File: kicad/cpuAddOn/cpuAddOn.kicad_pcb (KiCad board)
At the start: 6 copper layers, 60.6 x 100 mm, 138 parts, among them J1 QTE-020-01-X-D-A, J2 105450-0101, J3 Conn_01x05_Pin, J4 SJ-3551B-MSMT-TR-67, J5 TE_2311765-1, J7 Conn_02x13_Odd_Even, SW1 B3U-1000P[], SW2 B3U-1000P[], SW3 B3U-1000P[], SW4 B3U-1000P[]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

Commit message: Small revision on PCB
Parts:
- moved C23 1.45 mm to (101.7, 119.1)
- moved C24 1.45 mm to (102.4, 111.3)
- moved C26 1.45 mm to (94.2, 116.3)
- moved C27 1.45 mm to (98.0, 116.3)
- moved C28 1.45 mm to (99.9, 116.3)
- moved C29 1.45 mm to (93.2, 115.3)
- moved C30 1.45 mm to (93.2, 114.3)
- moved C31 1.45 mm to (93.2, 113.3)
- moved C32 1.45 mm to (93.2, 112.3)
- moved C34 1.45 mm to (104.0, 112.7)
- moved C38 1.45 mm to (91.0, 113.0)
- moved R28 1.45 mm to (104.6, 130.5)
- moved R29 1.45 mm to (96.1, 116.3)
- moved R30 1.45 mm to (102.7, 119.1)
- moved U9 1.45 mm to (98.4, 119.4)
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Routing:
- net CodecSDin: track 31.4 -> 64.6 mm
- net GND: track 222.6 -> 219.6 mm, vias 112 -> 111
- net Net-(U9-SLEEVE): track 22.2 -> 23.8 mm
- net SCL: track 90.6 -> 89.0 mm
- net SDA: track 103.5 -> 101.9 mm
- net Net-(U10-ROUTP): track 26.7 -> 28.2 mm
- net Net-(U10-LOUTP): track 22.8 -> 24.2 mm
- net Net-(U9-RING2): track 26.2 -> 27.7 mm
- net Net-(U3-PB2/BOOT1): track 4.21 -> 5.61 mm
- net Clock24MHz: track 111.4 -> 110.1 mm
- net Net-(U3-PB11): track 21.2 -> 22.2 mm
- net Presure_Irq: track 84.1 -> 84.7 mm
- net Net-(U10-JACKSNS/AUX): track 22.6 -> 23.1 mm
- net CodecSDout: track 30.4 -> 29.9 mm
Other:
- outline, holes or cut-outs redrawn

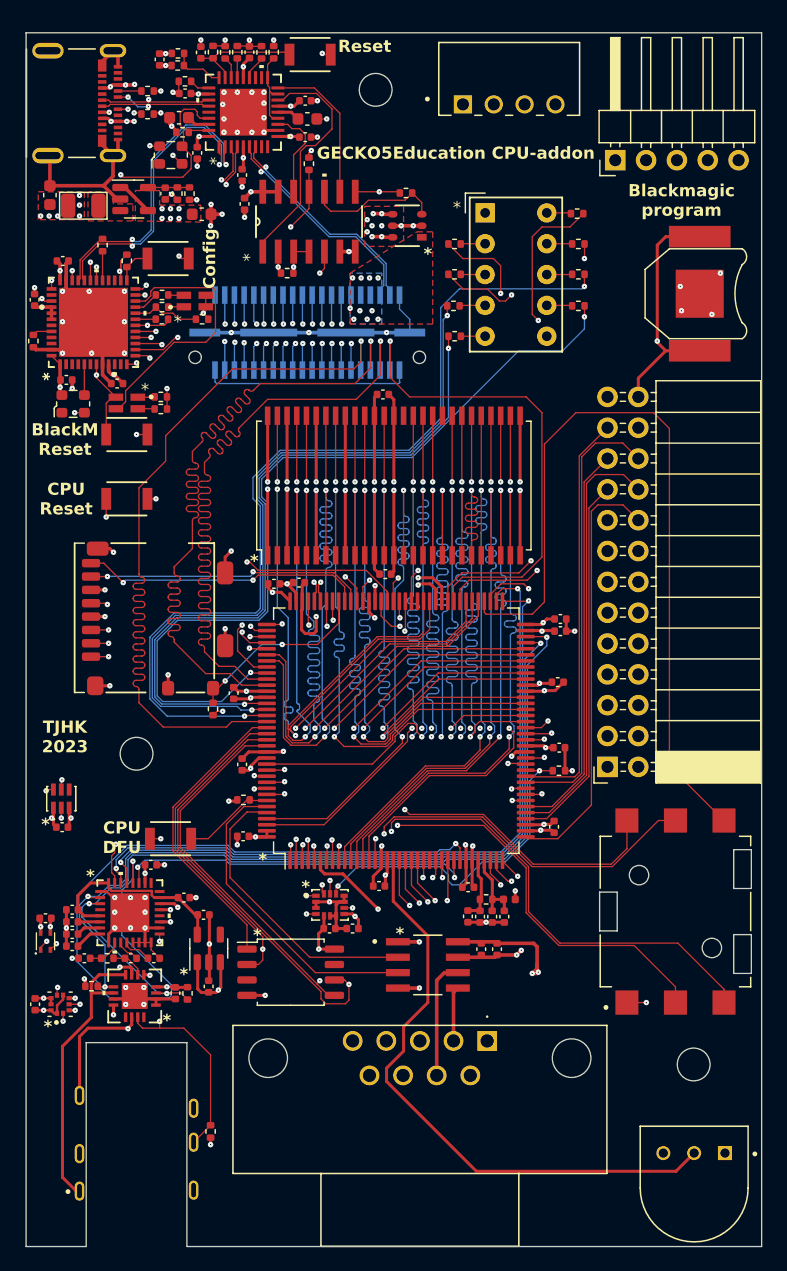
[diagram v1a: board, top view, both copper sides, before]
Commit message: fixed bug with RS232 Added support for bigger SDRAMs Changed 7-segment display to SMD and active low
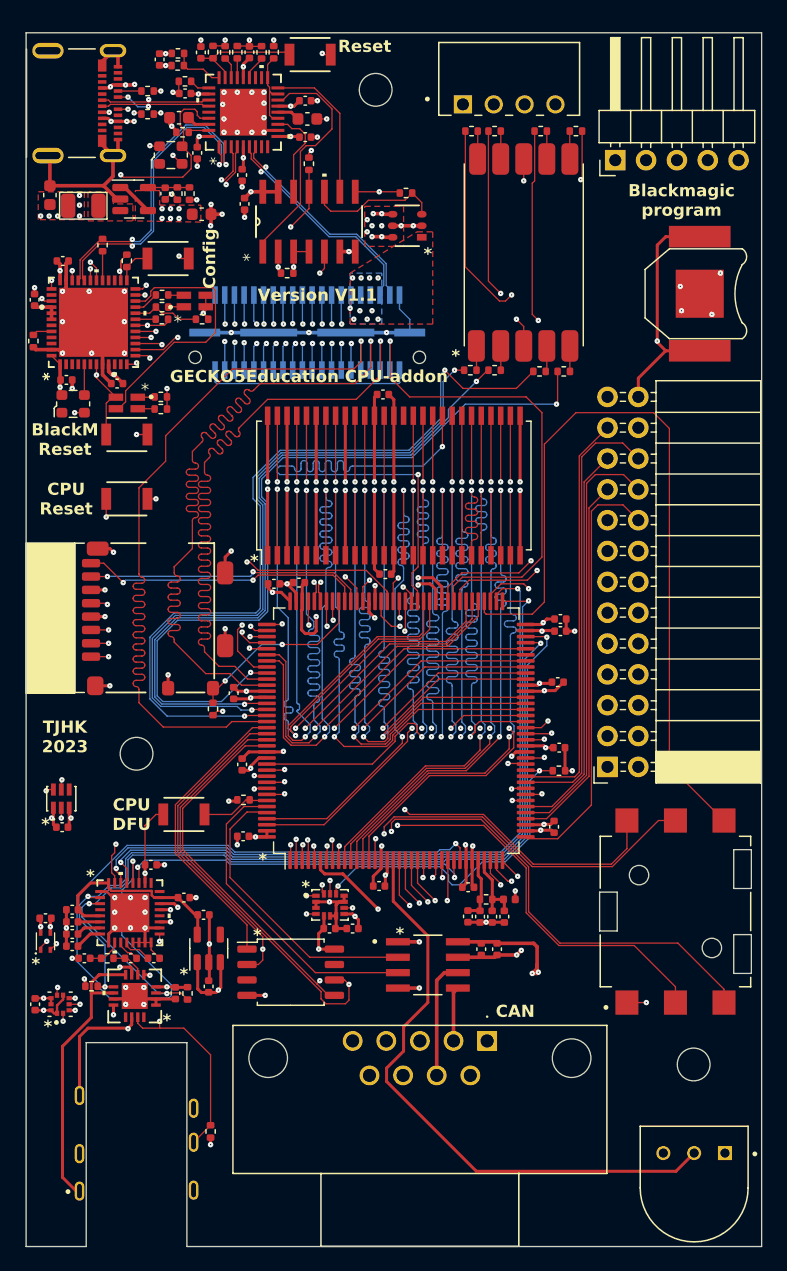
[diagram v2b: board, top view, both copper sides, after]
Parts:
- R35, R36, R37, R38, R39, R40, R41, R42: value 75R -> 62R
- U16: value HDSP-7403 -> HDSM-431W; footprint Display_7Segment:HDSP-7401 -> cpuAddOn:HDSM-431W
- U7: value AS4C4M16SA-6TAN -> AS4C16M16SA-6TAN
- moved R41 11.9 mm to (126.1, 48.1)
- moved U16 11.0 mm to (126.6, 65.8)
- moved R40 9.87 mm to (128.0, 48.1)
- moved R36 9.30 mm to (134.7, 48.1)
- moved R37 8.62 mm to (131.7, 67.9), turned to 0 degrees
- moved R35 7.43 mm to (131.8, 48.1), turned to 0 degrees
- moved R42 5.53 mm to (133.7, 67.9), turned to 0 degrees
- moved R39 5.48 mm to (126.0, 67.8)
- moved R38 4.32 mm to (128.0, 67.8)
- moved SW5 2.28 mm to (102.4, 104.4), turned to 180 degrees
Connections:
- SW5 pad 1: +3.3V -> Net-(U6-BOOT0)
- SW5 pad 2: Net-(U6-BOOT0) -> +3.3V
- U16 pad 1: GND -> Net-(U16-E)
- U16 pad 10: Net-(U16-A) -> Net-(U16-G)
- U16 pad 2: Net-(U16-F) -> Net-(U16-D)
- U16 pad 3: Net-(U16-G) -> +3.3V
- U16 pad 4: Net-(U16-E) -> Net-(U16-C)
- U16 pad 5: Net-(U16-D) -> Net-(U16-DP)
- U16 pad 6: GND -> Net-(U16-B)
- U16 pad 7: Net-(U16-DP) -> Net-(U16-A)
- U16 pad 8: Net-(U16-C) -> +3.3V
- U16 pad 9: Net-(U16-B) -> Net-(U16-F)
- U6 pad 101: BlackRxd -> BlackTxd
- U6 pad 102: BlackTxd -> BlackRxd
- U7 pad 36: unconnected-(U7-NC-Pad36) -> FMC_A12
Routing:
- net FMC_A12: track 0.00 -> 45.7 mm, vias 0 -> 2
- net Seg_C: track 76.6 -> 66.5 mm
- net Seg_G: track 42.4 -> 52.5 mm
- net +3.3V: track 144.6 -> 153.1 mm, vias 62 -> 63
- net Seg_B: track 39.0 -> 46.1 mm
- net Seg_F: track 45.1 -> 51.6 mm
- net Seg_E: track 62.8 -> 58.5 mm
- net Seg_DP: track 69.6 -> 65.7 mm
- net Seg_A: track 41.0 -> 44.8 mm
- net Net-(U6-BOOT0): track 7.51 -> 5.58 mm
- net Seg_D: track 59.8 -> 58.4 mm
- net Motion_Int1: track 55.8 -> 55.2 mm
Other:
- board text added: "CAN"
- board text added: "Version V1.1"

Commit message: Made V1.1 of the cpu-addon
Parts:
- added C56: 9pF, Capacitor_SMD:C_0402_1005Metric, F.Cu at (114.2, 112.3)
- added C57: 9pF, Capacitor_SMD:C_0402_1005Metric, F.Cu at (115.6, 112.3)
- added Y1: RT2012-32.768-9-20-EXT-TR, Crystal:Crystal_SMD_2012-2Pin_2.0x1.2mm, F.Cu at (114.9, 110.4)
- BT1: footprint Battery:BatteryHolder_Keystone_2998_1x6.8mm -> Battery:BatteryHolder_Keystone_1060_1x2032; moved to B.Cu
- J7: value Conn_02x13_Odd_Even -> Conn_02x16_Odd_Even; footprint Connector_PinSocket_2.54mm:PinSocket_2x13_P2.54mm_Horizontal -> Connector_PinSocket_2.54mm:PinSocket_2x16_P2.54mm_Horizontal
- U16: value HDSM-431W -> HDSM-433C
- moved BT1 55.3 mm to (119.0, 110.3), turned to 0 degrees
- moved C35 6.26 mm to (108.3, 112.5)
- moved C36 6.26 mm to (110.2, 112.5)
- moved U13 6.26 mm to (108.3, 110.5)
- moved C51 0.58 mm to (118.9, 110.7), turned to -90 degrees
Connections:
- J7 pad 1: GPIO1 -> +3.3V
- J7 pad 10: GPIO10 -> PMOD1_8
- J7 pad 11: GPIO11 -> PMOD1_1
- J7 pad 12: GPIO12 -> PMOD1_7
- J7 pad 13: GPIO13 -> ADC_PWM1
- J7 pad 14: GPIO14 -> ADC_PWM0
- J7 pad 15: GPIO15 -> ADC_PWM3
- J7 pad 16: GPIO16 -> ADC_PWM2
- J7 pad 17: GPIO17 -> ADC4
- J7 pad 18: GPIO18 -> GND
- J7 pad 19: GPIO19 -> +3.3V
- J7 pad 2: GPIO2 -> +3.3V
- J7 pad 20: GPIO20 -> +3.3V
- J7 pad 21: GPIO21 -> GND
- J7 pad 22: GPIO22 -> GND
- J7 pad 23: GPIO23 -> PMOD2_4
- J7 pad 24: +3.3V -> PMOD2_10
- J7 pad 25: GND -> PMOD2_3
- J7 pad 26: Net-(BT1-+) -> PMOD2_9
- J7 pad 3: GPIO3 -> GND
- J7 pad 4: GPIO4 -> GND
- J7 pad 5: GPIO5 -> PMOD1_4
- J7 pad 6: GPIO6 -> PMOD1_10
- J7 pad 7: GPIO7 -> PMOD1_3
- J7 pad 8: GPIO8 -> PMOD1_9
- J7 pad 9: GPIO9 -> PMOD1_2
- U16 pad 3: +3.3V -> GND
- U16 pad 8: +3.3V -> GND
- U6 pad 1: GPIO1 -> Joy3
- U6 pad 135: Joy3 -> PMOD1_2
- U6 pad 136: Joy4 -> PMOD1_9
- U6 pad 137: Joy5 -> PMOD1_10
- U6 pad 19: GPIO14 -> ADC4
- U6 pad 2: GPIO2 -> Joy4
- U6 pad 20: GPIO13 -> ADC_PWM2
- U6 pad 21: GPIO12 -> ADC_PWM3
- U6 pad 22: GPIO11 -> PMOD2_10
- U6 pad 26: GPIO10 -> PMOD2_9
- U6 pad 27: GPIO9 -> PMOD2_8
- U6 pad 3: GPIO3 -> Joy5
- U6 pad 34: GPIO15 -> PMOD2_1
- U6 pad 35: GPIO16 -> PMOD2_4
- U6 pad 36: GPIO17 -> PMOD2_2
- U6 pad 37: GPIO18 -> PMOD2_3
- U6 pad 4: GPIO4 -> PMOD1_7
- U6 pad 40: GPIO19 -> PMOD1_1
- U6 pad 41: GPIO20 -> PMOD1_4
- U6 pad 42: GPIO21 -> PMOD1_3
- U6 pad 46: GPIO22 -> ADC_PWM0
- U6 pad 47: GPIO23 -> ADC_PWM1
- U6 pad 5: GPIO5 -> PMOD1_8
- U6 pad 7: GPIO6 -> PMOD2_7
- U6 pad 8: GPIO7 -> Net-(U6-PC14)
- U6 pad 9: GPIO8 -> Net-(U6-PC15)
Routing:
- net PMOD2_7: track 0.00 -> 82.5 mm, vias 0 -> 1
- net PMOD2_8: track 0.00 -> 61.6 mm, vias 0 -> 1
- net PMOD2_9: track 0.00 -> 60.1 mm, vias 0 -> 1
- net PMOD2_10: track 0.00 -> 57.0 mm, vias 0 -> 1
- net ADC4: track 0.00 -> 54.8 mm, vias 0 -> 1
- net PMOD2_1: track 0.00 -> 52.4 mm, vias 0 -> 1
- net PMOD1_7: track 0.00 -> 52.2 mm, vias 0 -> 1
- net GPIO13: track 48.9 -> 0.00 mm, vias 1 -> 0
- net PMOD2_2: track 0.00 -> 48.5 mm, vias 0 -> 1
- net GPIO14: track 48.5 -> 0.00 mm, vias 1 -> 0
- net ADC_PWM3: track 0.00 -> 47.9 mm, vias 0 -> 1
- net ADC_PWM2: track 0.00 -> 47.7 mm, vias 0 -> 1
- net PMOD2_3: track 0.00 -> 47.2 mm
- net PMOD1_8: track 0.00 -> 46.7 mm, vias 0 -> 1
- net PMOD1_2: track 0.00 -> 45.1 mm, vias 0 -> 1
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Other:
- board text added: "+3V3"
- board text added: "GND"
- board text added: "PMOD1"
- board text added: "PMOD2"
- board text added: "SWCLK"
- board text added: "SWDIO"
- board text added: "SWO"

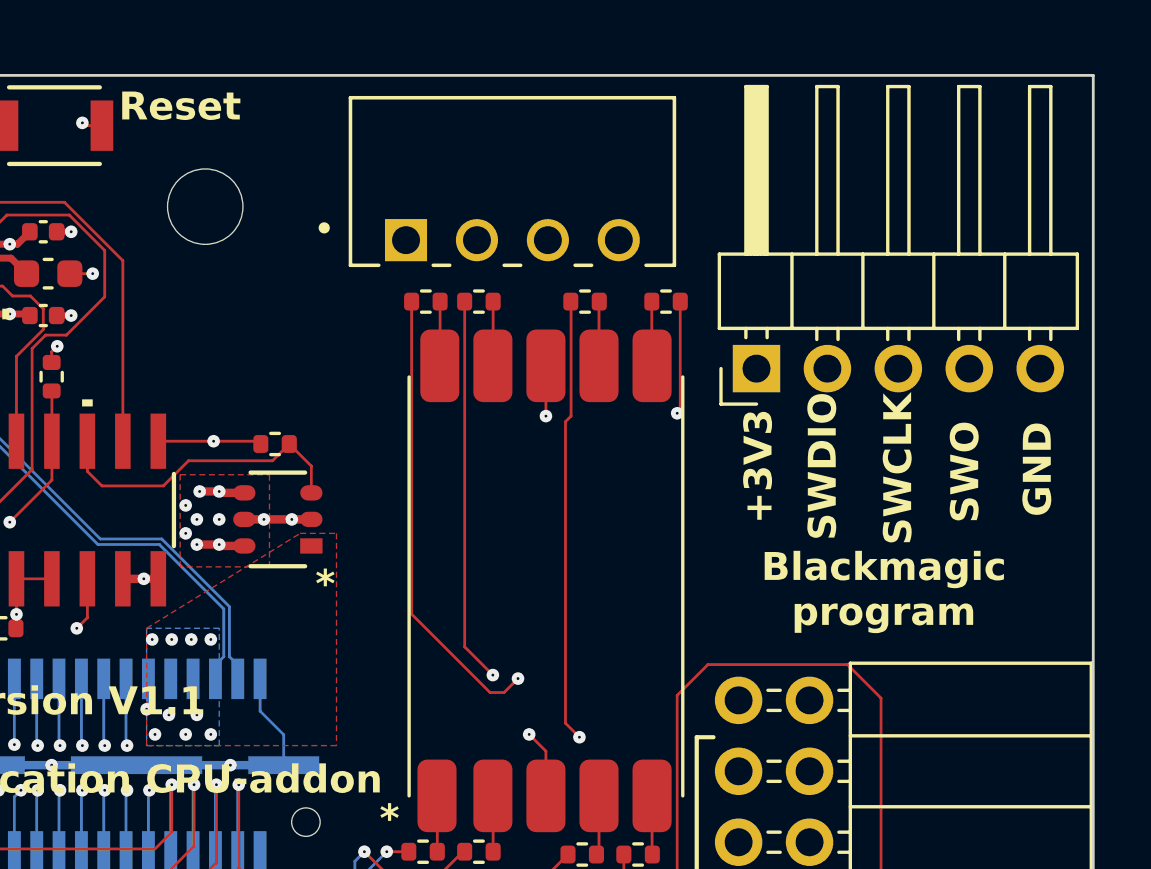
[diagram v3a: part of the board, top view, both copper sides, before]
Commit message: Added 2 add-on boards and updated GECKO5 to support olimex camera-OV7670 and an RTC.
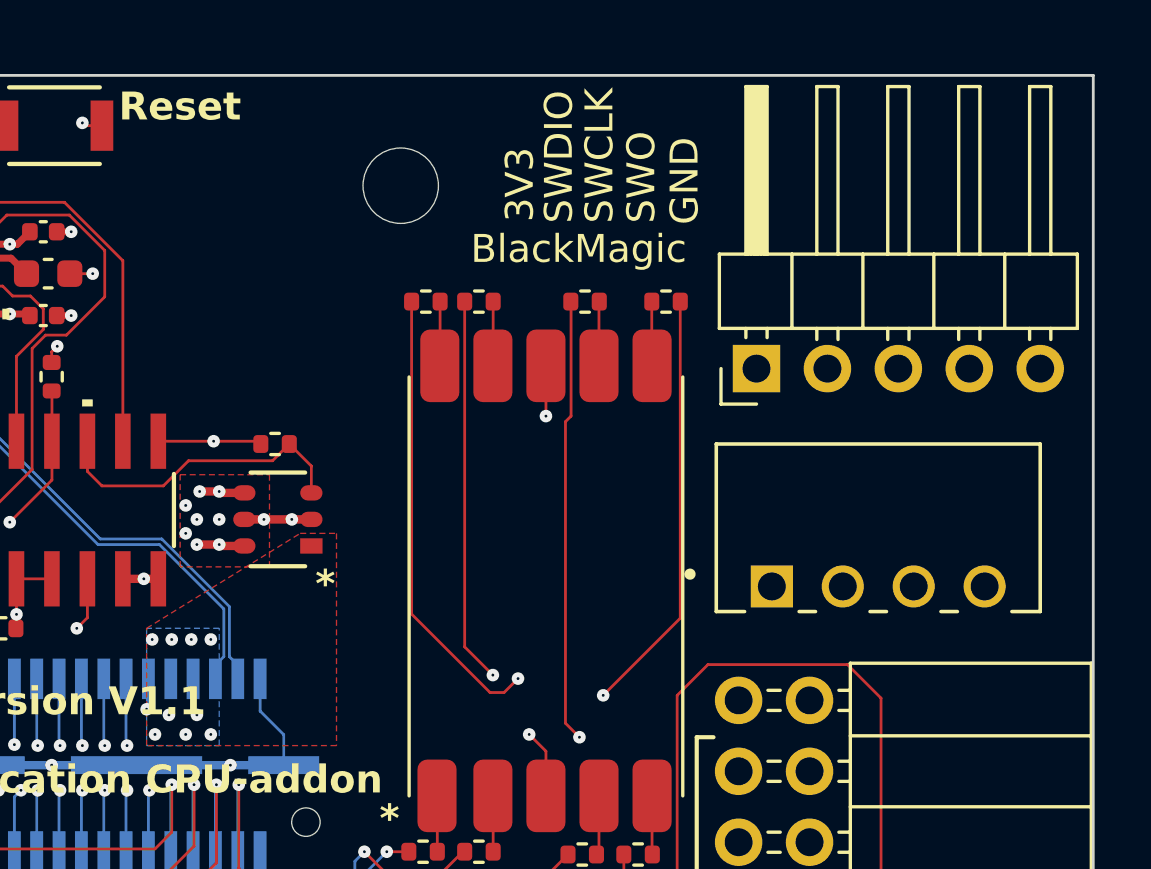
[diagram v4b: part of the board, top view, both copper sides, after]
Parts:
- moved PS1 18.0 mm to (142.3, 56.2)
- moved REF** 7.04 mm to (125.2, 44.0)
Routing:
- net Net-(PS1-0V): track 100.4 -> 77.4 mm
- net Net-(PS1-+VO): track 104.9 -> 82.0 mm
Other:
- board text added: "3V3"
- board text added: "BlackMagic"
- board text removed: "+3V3"
- board text removed: "Blackmagic program"
